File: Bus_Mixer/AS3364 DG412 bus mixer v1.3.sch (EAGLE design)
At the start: 121 parts, among them IC1 PCA9539PW, IC10 DG412-J, IC11 DG412-J, IC2 TL074JT, IC3 TL072JT, IC4 TL074JT, IC5 TL072JT, IC6 TL072JT, IC8 DG412-J, IC9 DG412-J

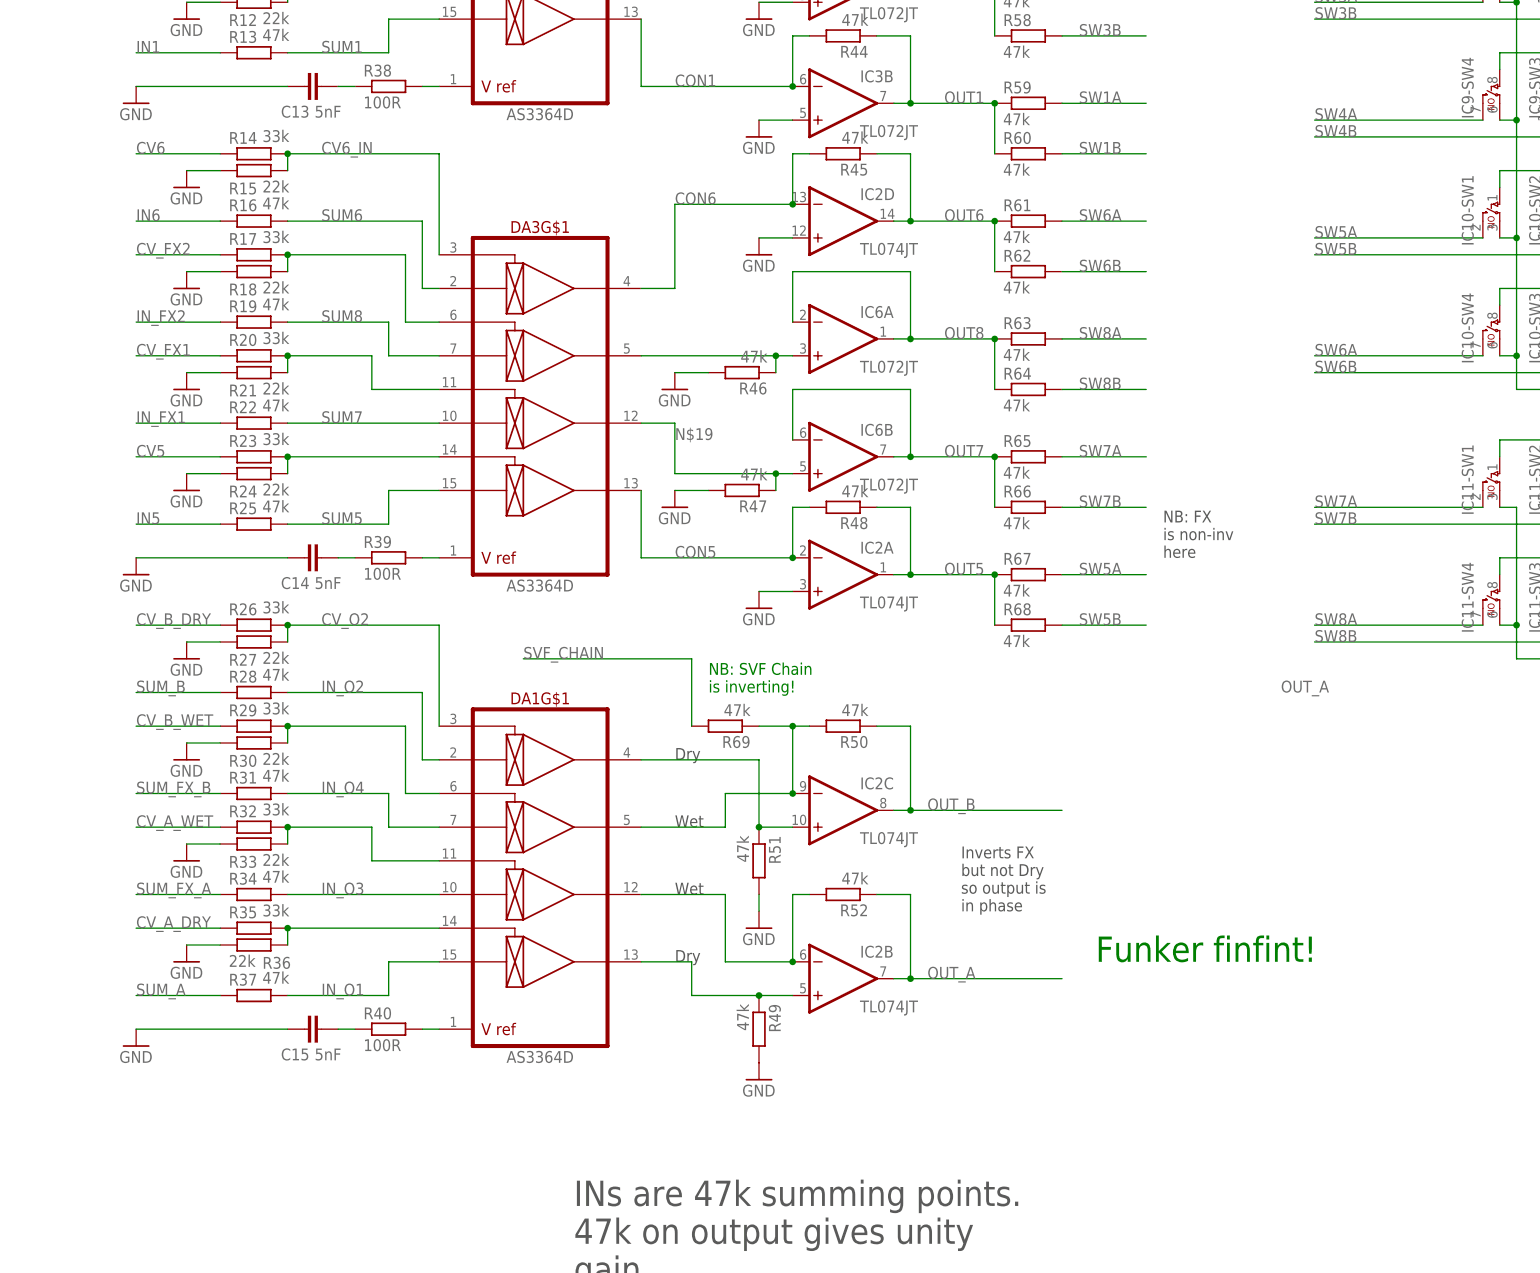
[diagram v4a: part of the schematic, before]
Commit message: Added increase-gain resistor to noise input
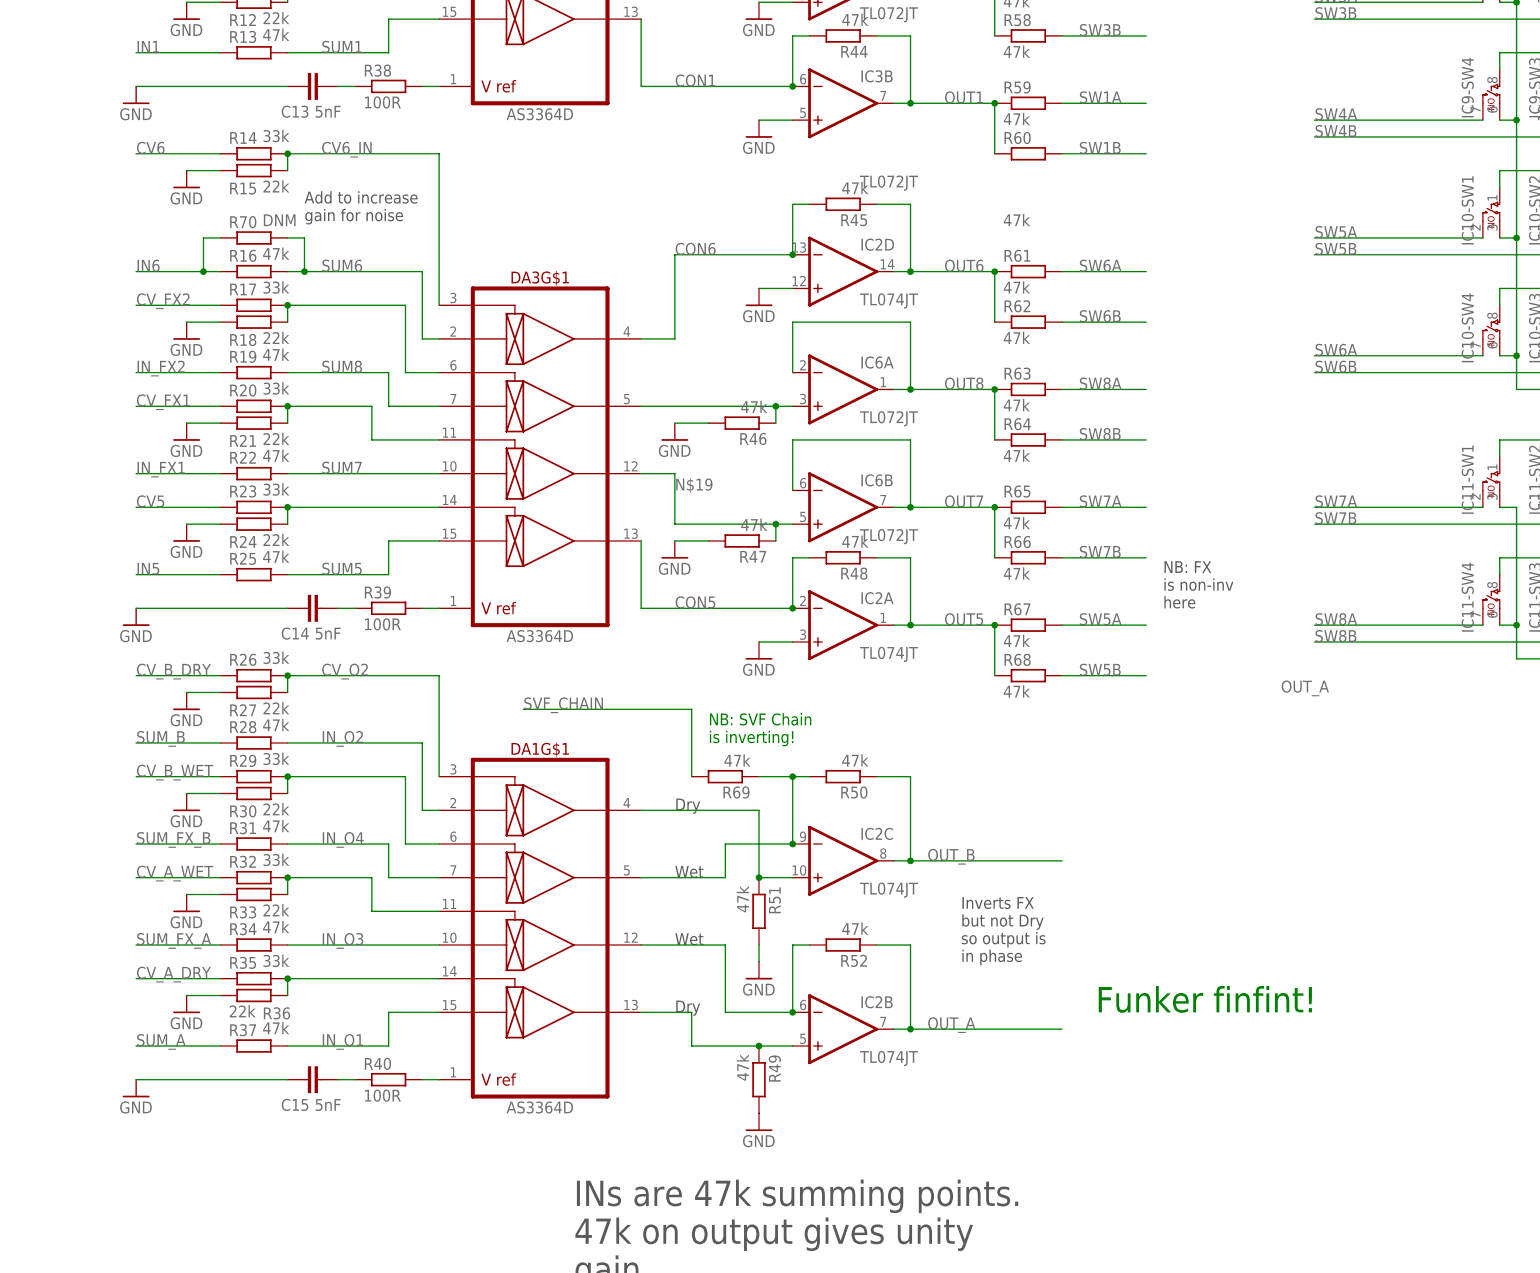
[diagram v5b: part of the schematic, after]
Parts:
- added R70: DNM, rcl:R-EU_R0805
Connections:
- net IN6: now also R70.1
- net SUM6: now also R70.2
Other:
- note added: "Add to increase gain for noise"
- moved on the sheet: C14, C15, DA1G$1, DA3G$1, IC2A, IC2B, IC2C, IC2D, IC6A, IC6B, R16, R17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

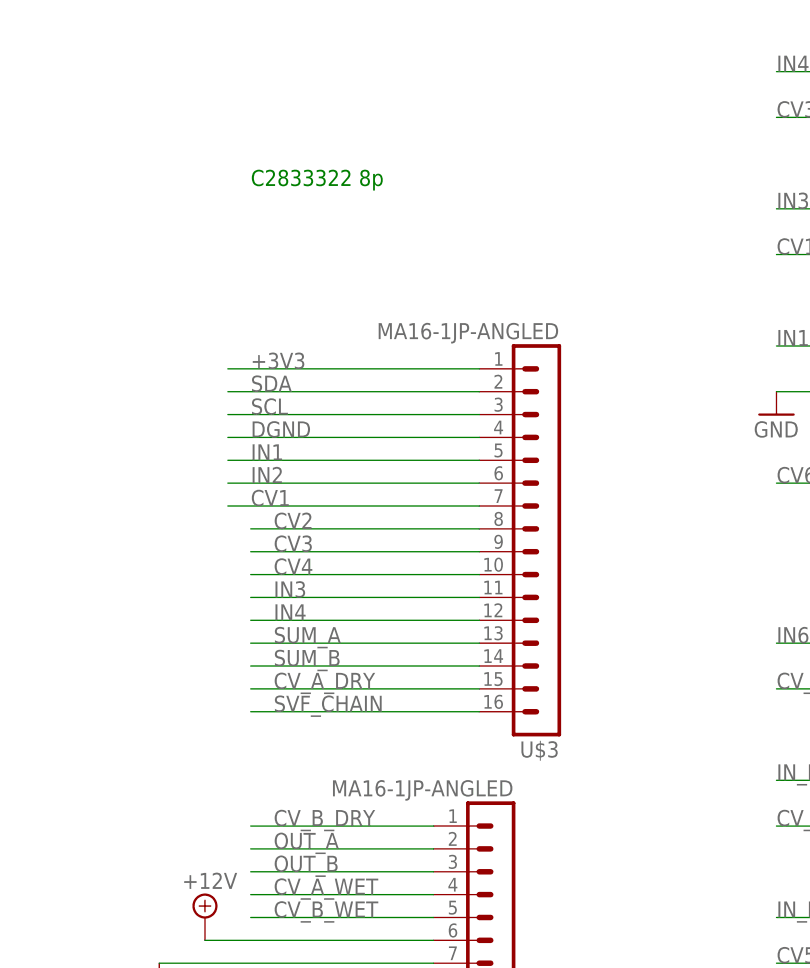
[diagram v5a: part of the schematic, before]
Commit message: Switched to female pin headers
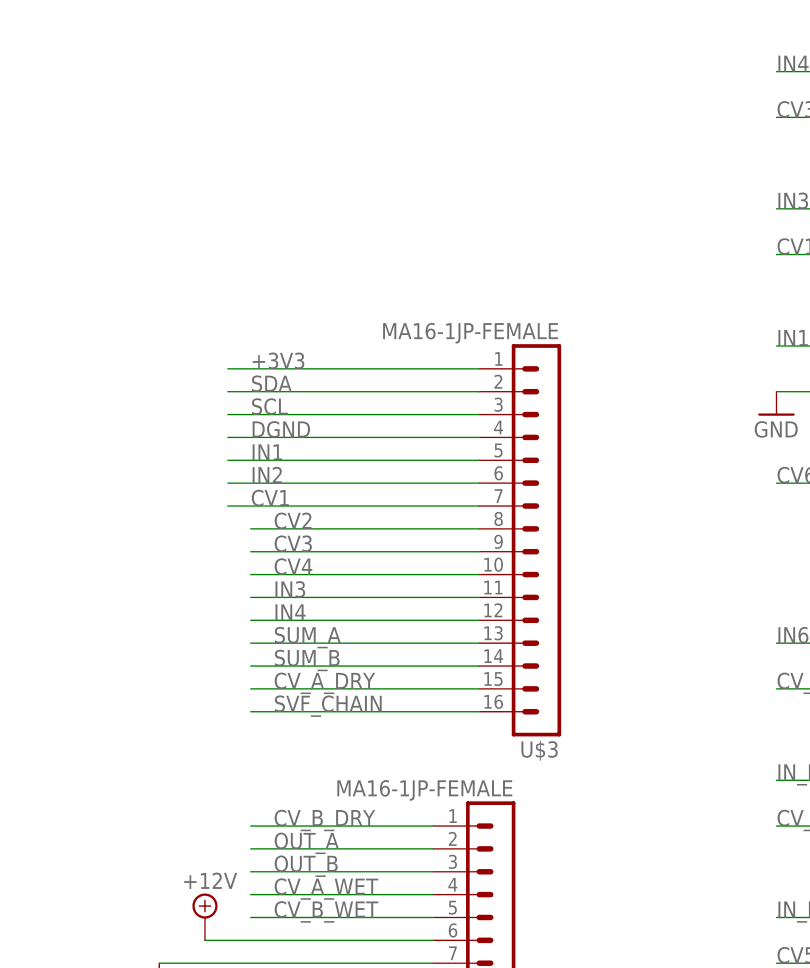
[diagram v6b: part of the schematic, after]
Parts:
- U$2, U$3: value MA16-1JP-ANGLED -> MA16-1JP-FEMALE
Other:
- note removed: "C2833322 8p"
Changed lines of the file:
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@@
 <part name="IC5" library="joakim" deviceset="TL072J" device="T" value="TL072JT"/>
 <part name="R69" library="rcl" library_urn="urn:adsk.eagle:library:334" deviceset="R-EU_" device="R0402" package3d_urn="urn:adsk.eagle:package:23547/3" value="47k"/>
-<part name="U$2" library="joakim" deviceset="MA16-1J" device="P" value="MA16-1JP-ANGLED"/>
-<part name="U$3" library="joakim" deviceset="MA16-1J" device="P" value="MA16-1JP-ANGLED"/>
+<part name="U$2" library="joakim" deviceset="MA16-1J" device="P" value="MA16-1JP-FEMALE"/>
+<part name="U$3" library="joakim" deviceset="MA16-1J" device="P" value="MA16-1JP-FEMALE"/>
 <part name="R70" library="rcl" library_urn="urn:adsk.eagle:library:334" deviceset="R-EU_" device="R0805" package3d_urn="urn:adsk.eagle:package:23553/2" value="DNM"/>
 </parts>
@@
 <text x="246.38" y="69.85" size="1.778" layer="97">Modules</text>
 <text x="247.65" y="63.5" size="1.778" layer="97">5V</text>
-<text x="-91.44" y="55.88" size="1.778" layer="91">C2833322 8p</text>
 <text x="264.16" y="38.1" size="1.778" layer="97">100kHz LPF</text>
 <text x="111.76" y="-106.68" size="3.81" layer="91">Funker finfint!</text>
